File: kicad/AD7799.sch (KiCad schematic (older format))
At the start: 0 parts

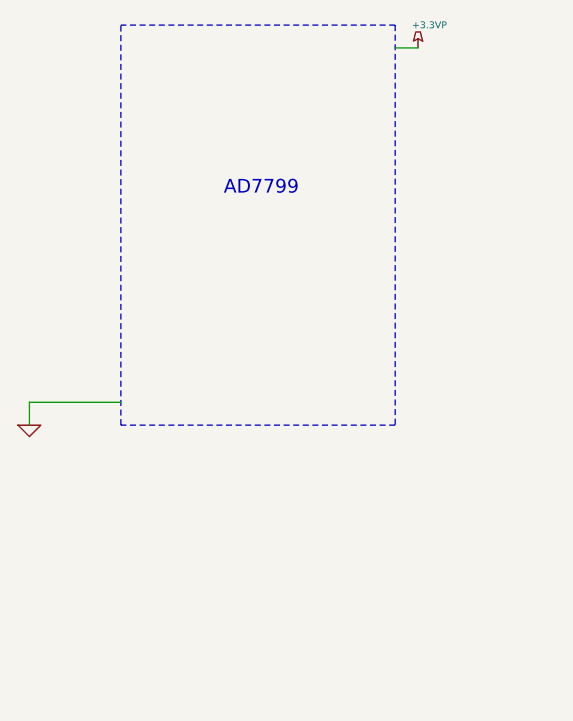
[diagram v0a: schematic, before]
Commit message: AD7799 symbol and AD77XX library
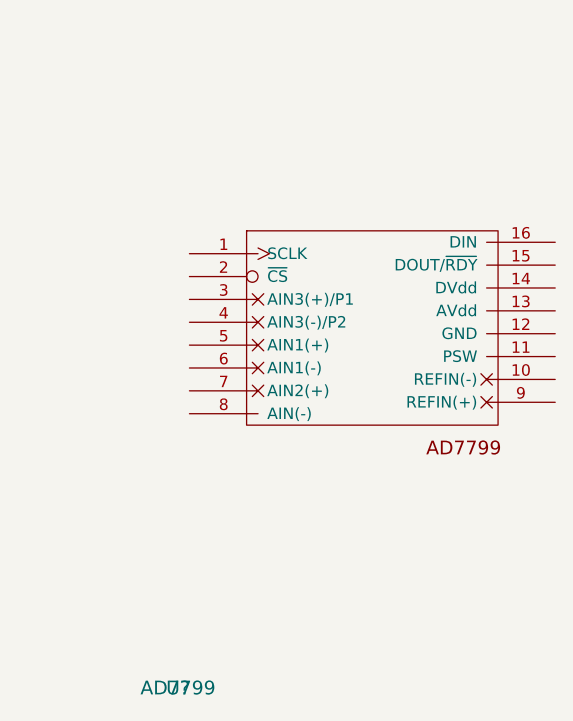
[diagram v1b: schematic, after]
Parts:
- added U?: AD7799, symbol AD7799
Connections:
- net labels removed: +3.3VP, GND
- wire segments 3 -> 0
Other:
- note removed: "AD7799\n"
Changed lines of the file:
@@
-EESchema Schematic File Version 2  date Sat 16 Nov 2013 05:35:54 AM PST
+EESchema Schematic File Version 2
 LIBS:power
 LIBS:device
@@
 LIBS:contrib
 LIBS:valves
-EELAYER 43  0
+LIBS:ad77xx
+LIBS:AD7799-cache
+EELAYER 24 0
 EELAYER END
-$Descr A4 11700 8267
+$Descr User 11000 8500
 encoding utf-8
 Sheet 1 1
-Title ""
+Title "AD7799 analog frontend"
 Date "16 nov 2013"
-Rev ""
+Rev "0.1"
 Comp ""
-Comment1 ""
+Comment1 "Minimal circuit"
 Comment2 ""
 Comment3 ""
 Comment4 ""
 $EndDescr
-Text Notes 4900 3350 0    60   ~ 0
-AD7799\n
-Wire Wire Line
-	4050 4350 4050 4250
-Wire Wire Line
-	4050 4250 4450 4250
-Wire Notes Line
-	5650 2600 4450 2600
-Wire Notes Line
-	5650 2600 5650 4350
-Wire Notes Line
-	5650 4350 4450 4350
-Wire Notes Line
-	4450 4350 4450 2600
-Wire Wire Line
-	5650 2700 5750 2700
 $Comp
-L GND #PWR?
-U 1 1 52877102
-P 4050 4350
-F 0 "#PWR?" H 4050 4350 30  0001 C CNN
-F 1 "GND" H 4050 4280 30  0001 C CNN
-	1    4050 4350
+L AD7799 U?
+U 1 1 5289229C
+P 4700 5500
+F 0 "U?" H 4700 5500 60  0000 C CNN
+F 1 "AD7799" H 4700 5500 60  0000 C CNN
+F 2 "" H 4700 5500 60  0000 C CNN
+F 3 "" H 4700 5500 60  0000 C CNN
+	1    4700 5500
 	1    0    0    -1
 $EndComp
-$Comp
-L +3.3VP #PWR?
-U 1 1 52876FDE
-P 5750 2700
-F 0 "#PWR?" H 5800 2730 20  0001 C CNN
-F 1 "+3.3VP" H 5800 2800 30  0000 C CNN
-	1    5750 2700
-	1    0    0    -1
-$EndComp
